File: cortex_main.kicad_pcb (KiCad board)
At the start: 2 copper layers, 119.4 x 119.4 mm, 24 parts, among them P1 CONN_01X05, P10 CONN_01X03, P11 CONN_01X03, P12 CONN_01X03, P13 CONN_01X03, P14 CONN_01X03, P15 CONN_01X03, P16 CONN_01X02, P17 CONN_01X02, P2 CONN_02X04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

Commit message: cortex: pcb move on
some new stuff. sd21, and few routing tests

Signed-off-by: Yannick Gicquel <ygicquel@gmail.com>
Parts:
- P5: footprint Terminal_Blocks:TerminalBlock_Pheonix_MKDS1.5-2pol -> Pin_Headers:Pin_Header_Straight_1x02_Pitch2.54mm
- moved P5 60.2 mm to (105.4, 113.0), turned to 180 degrees
- moved P4 44.4 mm to (105.4, 118.1)
- moved P6 6.35 mm to (100.3, 113.0)
- moved P7 5.08 mm to (73.7, 113.0)
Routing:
- net +5V: track 0.00 -> 138.2 mm
- net /Sheet_Connectors/SCL_C: track 0.00 -> 25.0 mm
- net /Sheet_Connectors/SDA_C: track 0.00 -> 20.6 mm
- net /Sheet_Connectors/UART_DBG_TXD: track 0.00 -> 18.8 mm
- net /Sheet_Connectors/SCL_D: track 0.00 -> 17.6 mm
- net /Sheet_Connectors/UART_DBG_RXD: track 0.00 -> 14.5 mm
- net /Sheet_Connectors/SDA_D: track 0.00 -> 13.2 mm
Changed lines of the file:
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@@
   (general
     (links 102)
-    (no_connects 79)
+    (no_connects 67)
     (area 35.484999 49.454999 155.015001 168.985001)
     (thickness 1.6)
     (drawings 9)
-    (tracks 4)
+    (tracks 39)
     (zones 0)
     (modules 24)
@@
   )
   (module Pin_Headers:Pin_Header_Straight_1x04_Pitch2.54mm (layer F.Cu)
-    (at 146.05 135.89)
+    (at 105.41 118.11)
     (descr "Through hole straight pin header, 1x04, 2.54mm pitch, single row")
     (tags "Through hole pin header THT 1x04 2.54mm single row")
@@
       (scale (xyz 1 1 1))
       (rotate (xyz 0 0 90))
-    )
-  )
-  (module Terminal_Blocks:TerminalBlock_Pheonix_MKDS1.5-2pol (layer F.Cu)
-    (at 147.32 156.21 90)
-    (descr "2-way 5mm pitch terminal block, Phoenix MKDS series")
-    (fp_text reference P5 (at 2.5 5.9 90) (layer F.SilkS)
-      (effects (font (size 1 1) (thickness 0.15)))
-    )
-    (fp_text value CONN_01X02 (at 2.5 -6.6 90) (layer F.Fab)
-      (effects (font (size 1 1) (thickness 0.15)))
-    )
-    (fp_line (start -2.7 -5.4) (end 7.7 -5.4) (layer F.CrtYd) (width 0.05))
-    (fp_line (start -2.7 4.8) (end -2.7 -5.4) (layer F.CrtYd) (width 0.05))
-    (fp_line (start 7.7 4.8) (end -2.7 4.8) (layer F.CrtYd) (width 0.05))
-    (fp_line (start 7.7 -5.4) (end 7.7 4.8) (layer F.CrtYd) (width 0.05))
-    (fp_line (start 2.5 4.1) (end 2.5 4.6) (layer F.SilkS) (width 0.15))
-    (fp_circle (center 5 0.1) (end 3 0.1) (layer F.SilkS) (width 0.15))
-    (fp_circle (center 0 0.1) (end 2 0.1) (layer F.SilkS) (width 0.15))
-    (fp_line (start -2.5 2.6) (end 7.5 2.6) (layer F.SilkS) (width 0.15))
-    (fp_line (start -2.5 -2.3) (end 7.5 -2.3) (layer F.SilkS) (width 0.15))
-    (fp_line (start -2.5 4.1) (end 7.5 4.1) (layer F.SilkS) (width 0.15))
-    (fp_line (start -2.5 4.6) (end 7.5 4.6) (layer F.SilkS) (width 0.15))
-    (fp_line (start 7.5 4.6) (end 7.5 -5.2) (layer F.SilkS) (width 0.15))
-    (fp_line (start 7.5 -5.2) (end -2.5 -5.2) (layer F.SilkS) (width 0.15))
-    (fp_line (start -2.5 -5.2) (end -2.5 4.6) (layer F.SilkS) (width 0.15))
-    (pad 1 thru_hole rect (at 0 0 90) (size 2.5 2.5) (drill 1.3) (layers *.Cu *.Mask)
-      (net 34 GND))
-    (pad 2 thru_hole circle (at 5 0 90) (size 2.5 2.5) (drill 1.3) (layers *.Cu *.Mask)
-      (net 48 +5V))
-    (model Terminal_Blocks.3dshapes/TerminalBlock_Pheonix_MKDS1.5-2pol.wrl
-      (at (xyz 0.0984 0 0))
-      (scale (xyz 1 1 1))
-      (rotate (xyz 0 0 0))
     )
   )
@@
   )
   (module Pin_Headers:Pin_Header_Straight_1x06_Pitch2.54mm (layer F.Cu)
-    (at 93.98 113.03)
+    (at 100.33 113.03)
     (descr "Through hole straight pin header, 1x06, 2.54mm pitch, single row")
     (tags "Through hole pin header THT 1x06 2.54mm single row")
@@
   )
   (module Pin_Headers:Pin_Header_Straight_1x06_Pitch2.54mm (layer F.Cu)
-    (at 68.58 113.03)
+    (at 73.66 113.03)
     (descr "Through hole straight pin header, 1x06, 2.54mm pitch, single row")
     (tags "Through hole pin header THT 1x06 2.54mm single row")
@@
     )
   )
+  (module Pin_Headers:Pin_Header_Straight_1x02_Pitch2.54mm (layer F.Cu)
+    (at 105.41 113.03 180)
+    (descr "Through hole straight pin header, 1x02, 2.54mm pitch, single row")
+    (tags "Through hole pin header THT 1x02 2.54mm single row")
+    (fp_text reference P5 (at 0 -2.39 180) (layer F.SilkS)
+      (effects (font (size 1 1) (thickness 0.15)))
+    )
+    (fp_text value CONN_01X02 (at 0 4.93 180) (layer F.Fab)
+      (effects (font (size 1 1) (thickness 0.15)))
+    )
+    (fp_line (start -1.27 -1.27) (end -1.27 3.81) (layer F.Fab) (width 0.1))
+    (fp_line (start -1.27 3.81) (end 1.27 3.81) (layer F.Fab) (width 0.1))
+    (fp_line (start 1.27 3.81) (end 1.27 -1.27) (layer F.Fab) (width 0.1))
+    (fp_line (start 1.27 -1.27) (end -1.27 -1.27) (layer F.Fab) (width 0.1))
+    (fp_line (start -1.39 1.27) (end -1.39 3.93) (layer F.SilkS) (width 0.12))
+    (fp_line (start -1.39 3.93) (end 1.39 3.93) (layer F.SilkS) (width 0.12))
+    (fp_line (start 1.39 3.93) (end 1.39 1.27) (layer F.SilkS) (width 0.12))
+    (fp_line (start 1.39 1.27) (end -1.39 1.27) (layer F.SilkS) (width 0.12))
+    (fp_line (start -1.39 0) (end -1.39 -1.39) (layer F.SilkS) (width 0.12))
+    (fp_line (start -1.39 -1.39) (end 0 -1.39) (layer F.SilkS) (width 0.12))
+    (fp_line (start -1.6 -1.6) (end -1.6 4.1) (layer F.CrtYd) (width 0.05))
+    (fp_line (start -1.6 4.1) (end 1.6 4.1) (layer F.CrtYd) (width 0.05))
+    (fp_line (start 1.6 4.1) (end 1.6 -1.6) (layer F.CrtYd) (width 0.05))
+    (fp_line (start 1.6 -1.6) (end -1.6 -1.6) (layer F.CrtYd) (width 0.05))
+    (pad 1 thru_hole rect (at 0 0 180) (size 1.7 1.7) (drill 1) (layers *.Cu *.Mask)
+      (net 34 GND))
+    (pad 2 thru_hole oval (at 0 2.54 180) (size 1.7 1.7) (drill 1) (layers *.Cu *.Mask)
+      (net 48 +5V))
+    (model Pin_Headers.3dshapes/Pin_Header_Straight_1x02_Pitch2.54mm.wrl
+      (at (xyz 0 -0.05 0))
+      (scale (xyz 1 1 1))
+      (rotate (xyz 0 0 90))
+    )
+  )
   (gr_line (start 35.56 49.53) (end 154.94 49.53) (angle 90) (layer Edge.Cuts) (width 0.15))
   (gr_line (start 154.94 168.91) (end 154.94 49.53) (angle 90) (layer Edge.Cuts) (width 0.15))
@@
   (gr_circle (center 151.13 165.1) (end 152.4 165.1) (layer Edge.Cuts) (width 0.15))
   (gr_circle (center 39.37 165.1) (end 40.64 165.1) (layer Edge.Cuts) (width 0.15))
-  (segment (start 109.22 62.23) (end 109.22 54.61) (width 3) (layer B.Cu) (net 33) (status 400000))
+  (segment (start 109.22 62.23) (end 109.22 54.61) (width 3) (layer B.Cu) (net 33))
   (segment (start 92.71 52.07) (end 92.71 53.34) (width 3) (layer B.Cu) (net 33))
   (segment (start 106.68 52.07) (end 92.71 52.07) (width 3) (layer B.Cu) (net 33))
   (segment (start 109.22 54.61) (end 106.68 52.07) (width 3) (layer B.Cu) (net 33))
+  (segment (start 91.44 132.08) (end 91.44 120.65) (width 0.25) (layer B.Cu) (net 37))
+  (segment (start 88.9 118.11) (end 85.09 118.11) (width 0.25) (layer B.Cu) (net 37))
+  (segment (start 91.44 120.65) (end 88.9 118.11) (width 0.25) (layer B.Cu) (net 37))
+  (segment (start 88.9 132.08) (end 88.9 121.92) (width 0.25) (layer B.Cu) (net 38))
+  (segment (start 87.63 120.65) (end 85.09 120.65) (width 0.25) (layer B.Cu) (net 38))
+  (segment (start 88.9 121.92) (end 87.63 120.65) (width 0.25) (layer B.Cu) (net 38))
+  (segment (start 132.08 93.345) (end 149.225 93.345) (width 0.25) (layer B.Cu) (net 48))
+  (segment (start 152.4 67.31) (end 147.32 62.23) (width 0.25) (layer B.Cu) (net 48))
+  (segment (start 152.4 90.17) (end 152.4 67.31) (width 0.25) (layer B.Cu) (net 48))
+  (segment (start 149.225 93.345) (end 152.4 90.17) (width 0.25) (layer B.Cu) (net 48))
+  (segment (start 129.54 166.37) (end 132.08 166.37) (width 0.25) (layer B.Cu) (net 48))
+  (segment (start 132.08 166.37) (end 134.62 166.37) (width 0.25) (layer B.Cu) (net 48))
+  (segment (start 134.62 166.37) (end 143.51 166.37) (width 0.25) (layer B.Cu) (net 48))
+  (segment (start 143.51 166.37) (end 151.13 158.75) (width 0.25) (layer B.Cu) (net 48))
+  (segment (start 151.13 158.75) (end 151.13 125.73) (width 0.25) (layer B.Cu) (net 48))
+  (segment (start 151.13 125.73) (end 146.05 120.65) (width 0.25) (layer B.Cu) (net 48))
+  (segment (start 146.05 120.65) (end 124.46 120.65) (width 0.25) (layer B.Cu) (net 48))
+  (segment (start 105.41 120.65) (end 104.14 120.65) (width 0.25) (layer B.Cu) (net 52))
+  (segment (start 101.6 118.11) (end 100.33 118.11) (width 0.25) (layer B.Cu) (net 52))
+  (segment (start 104.14 120.65) (end 101.6 118.11) (width 0.25) (layer B.Cu) (net 52))
+  (segment (start 100.33 118.11) (end 96.52 118.11) (width 0.25) (layer B.Cu) (net 52))
+  (segment (start 93.98 120.65) (end 93.98 132.08) (width 0.25) (layer B.Cu) (net 52))
+  (segment (start 96.52 118.11) (end 93.98 120.65) (width 0.25) (layer B.Cu) (net 52))
+  (segment (start 105.41 123.19) (end 104.14 123.19) (width 0.25) (layer B.Cu) (net 53))
+  (segment (start 101.6 120.65) (end 100.33 120.65) (width 0.25) (layer B.Cu) (net 53))
+  (segment (start 104.14 123.19) (end 101.6 120.65) (width 0.25) (layer B.Cu) (net 53))
+  (segment (start 96.52 132.08) (end 96.52 121.92) (width 0.25) (layer B.Cu) (net 53))
+  (segment (start 97.79 120.65) (end 100.33 120.65) (width 0.25) (layer B.Cu) (net 53))
+  (segment (start 96.52 121.92) (end 97.79 120.65) (width 0.25) (layer B.Cu) (net 53))
+  (segment (start 73.66 118.11) (end 71.12 118.11) (width 0.25) (layer B.Cu) (net 56))
+  (segment (start 68.58 120.65) (end 68.58 132.08) (width 0.25) (layer B.Cu) (net 56))
+  (segment (start 71.12 118.11) (end 68.58 120.65) (width 0.25) (layer B.Cu) (net 56))
+  (segment (start 73.66 120.65) (end 72.39 120.65) (width 0.25) (layer B.Cu) (net 57))
+  (segment (start 71.12 121.92) (end 71.12 132.08) (width 0.25) (layer B.Cu) (net 57))
+  (segment (start 72.39 120.65) (end 71.12 121.92) (width 0.25) (layer B.Cu) (net 57))
   (zone (net 69) (net_name OUTB_L) (layer B.Cu) (hatch edge 0.508)
     (connect_pads yes (clearance 1.016))

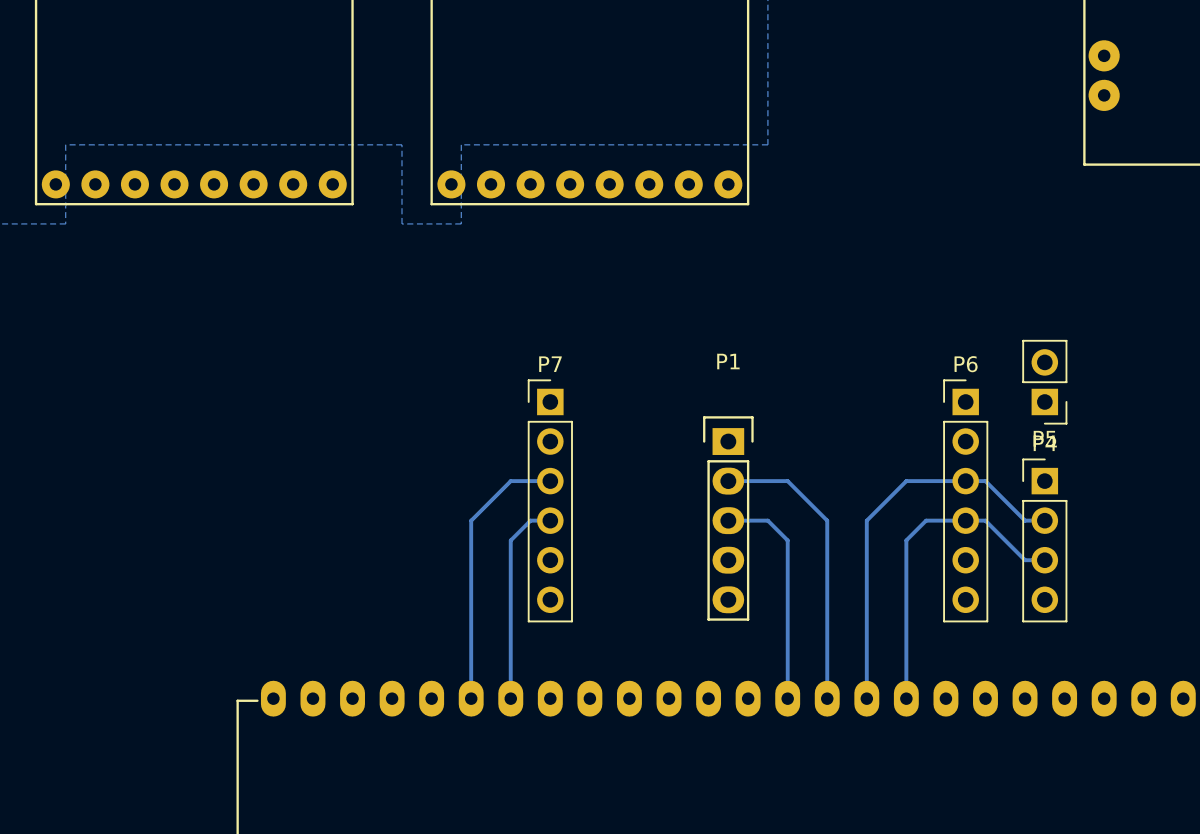
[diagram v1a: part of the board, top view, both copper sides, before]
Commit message: cortex: new pin muxing to ease pcb layout
pcb layout progress as well

Signed-off-by: Yannick Gicquel <ygicquel@gmail.com>
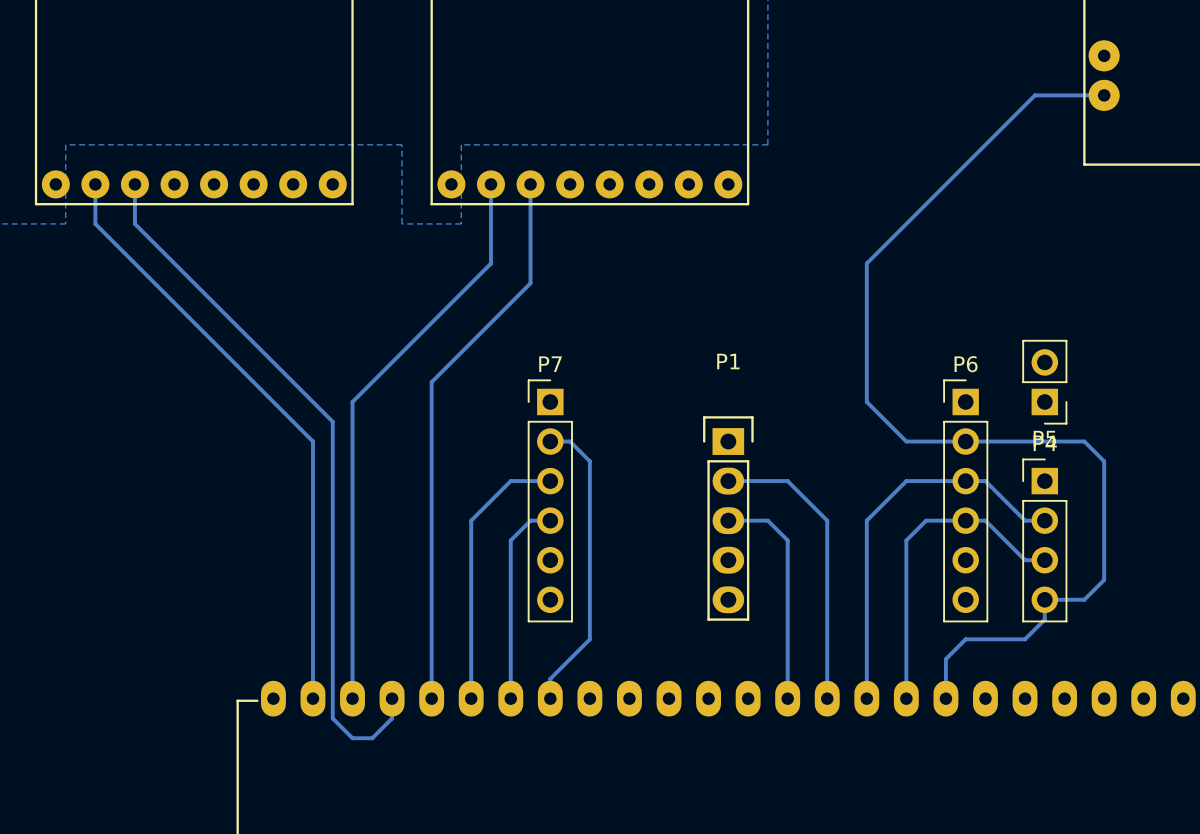
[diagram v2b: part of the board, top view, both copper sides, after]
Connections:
- U1 pad 20: Net-(U1-Pad20) -> /Sheet_Connectors/RGB_LEDEN_L
- U1 pad 23: Net-(U1-Pad23) -> /Sheet_Connectors/RGB_LEDEN_R
- U1 pad 28: /Sheet_Connectors/RGB_LEDEN_L -> /Sheet_MCU/PWM_R
- U1 pad 29: /Sheet_Connectors/RGB_LEDEN_R -> /Sheet_MCU/PWM_L
- U1 pad 30: /Sheet_MCU/DIR_L -> /Sheet_MCU/DIR_R
- U1 pad 31: /Sheet_MCU/DIR_R -> /Sheet_MCU/DIR_L
- U1 pad 36: /Sheet_MCU/PWM_L -> Net-(U1-Pad36)
- U1 pad 37: /Sheet_MCU/PWM_R -> Net-(U1-Pad37)
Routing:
- net +3V3: track 0.00 -> 87.9 mm
- net /Sheet_MCU/PWM_L: track 0.00 -> 45.7 mm
- net /Sheet_MCU/DIR_L: track 0.00 -> 38.8 mm
- net /Sheet_MCU/DIR_R: track 0.00 -> 36.7 mm
- net /Sheet_MCU/PWM_R: track 0.00 -> 35.7 mm

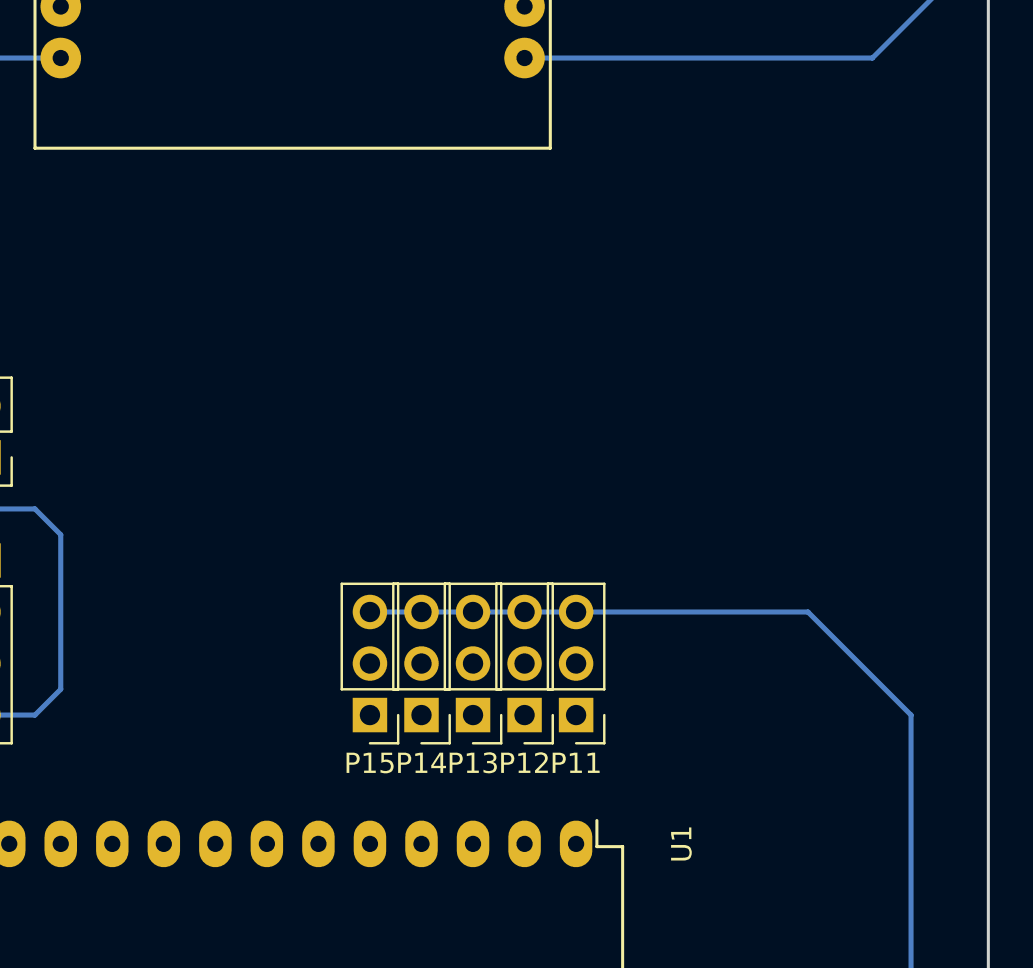
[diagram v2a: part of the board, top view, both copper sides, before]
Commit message: cortex: add Arms Motor mosfet drivers
Signed-off-by: Yannick Gicquel <ygicquel@gmail.com>
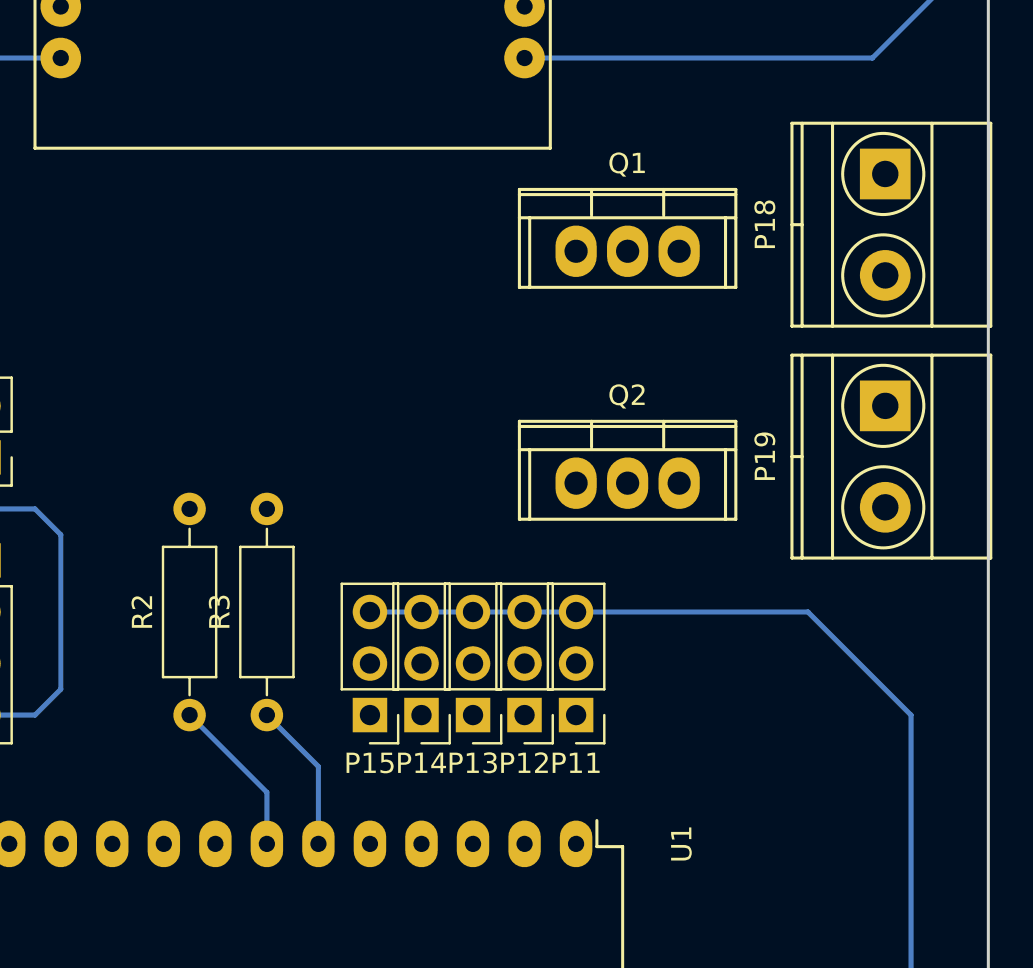
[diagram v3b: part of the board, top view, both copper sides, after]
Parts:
- added P18: CONN_01X02, Terminal_Blocks:TerminalBlock_Pheonix_MKDS1.5-2pol, F.Cu at (149.9, 99.1)
- added P19: CONN_01X02, Terminal_Blocks:TerminalBlock_Pheonix_MKDS1.5-2pol, F.Cu at (149.9, 110.5)
- added Q1: IRF540N, Power_Integrations:TO-220, F.Cu at (137.2, 102.9)
- added Q2: IRF540N, Power_Integrations:TO-220, F.Cu at (137.2, 114.3)
- added R2: 100R, Resistors_ThroughHole:R_Axial_DIN0207_L6.3mm_D2.5mm_P10.16mm_Horizontal, F.Cu at (115.6, 125.7)
- added R3: 100R, Resistors_ThroughHole:R_Axial_DIN0207_L6.3mm_D2.5mm_P10.16mm_Horizontal, F.Cu at (119.4, 125.7)
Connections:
- U1 pad 6: Net-(U1-Pad6) -> /Sheet_MCU/CMD_ARMMOTOR_R
- U1 pad 7: Net-(U1-Pad7) -> /Sheet_MCU/CMD_ARMMOTOR_L
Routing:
- net /Sheet_MCU/CMD_ARMMOTOR_L: track 0.00 -> 7.93 mm
- net /Sheet_MCU/CMD_ARMMOTOR_R: track 0.00 -> 7.40 mm
